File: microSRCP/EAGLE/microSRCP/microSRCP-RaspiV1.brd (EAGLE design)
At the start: 61 x 55.9 mm, 19 parts

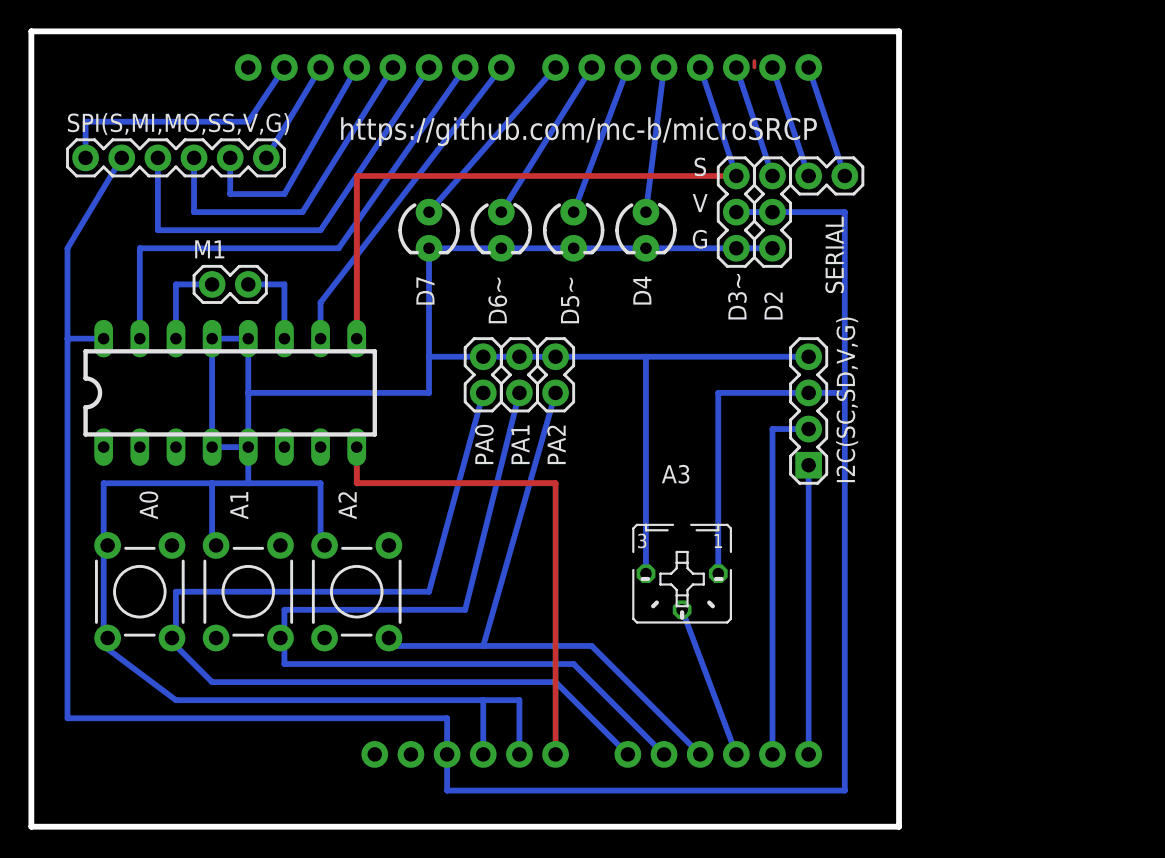
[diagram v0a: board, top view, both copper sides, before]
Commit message: Schaltplaene und Layout von eigenen Shields
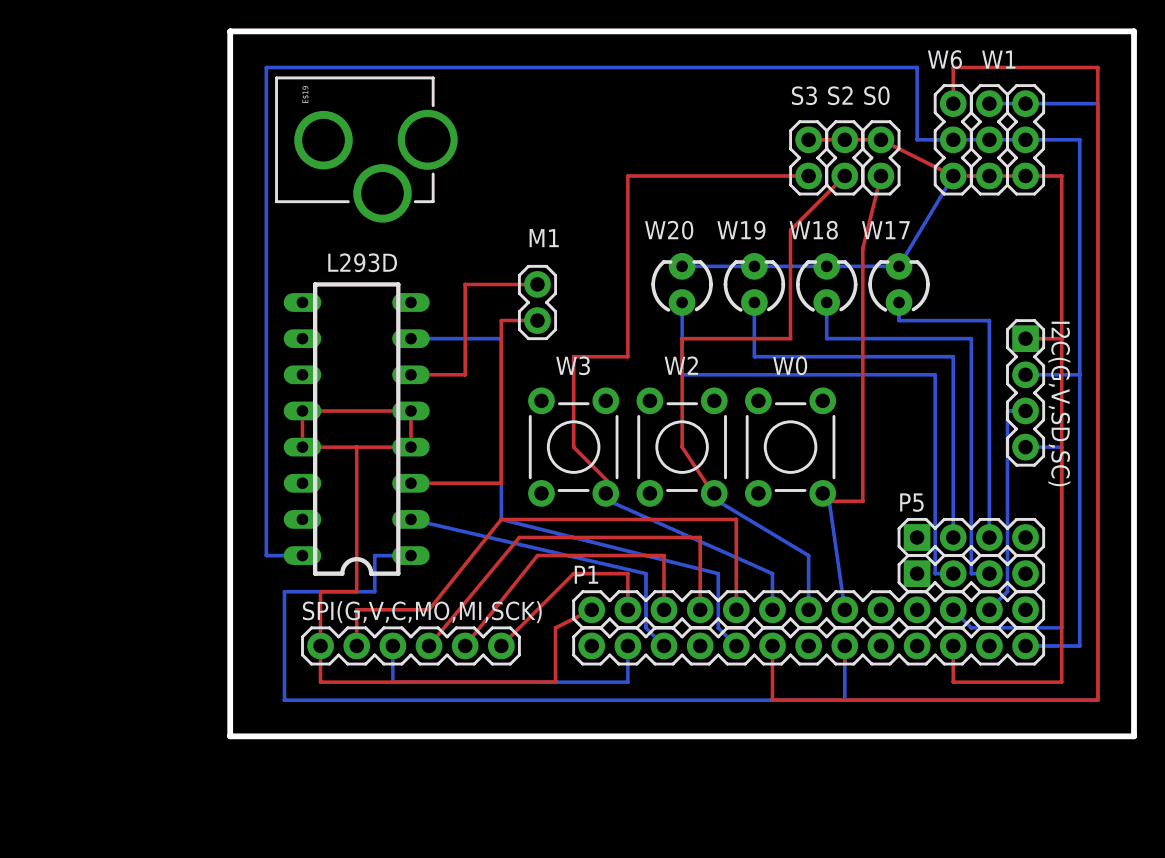
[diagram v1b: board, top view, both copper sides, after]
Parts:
- removed 1: L293D(D3~,D8,D9), SparkFun-AnalogIC:DIL16
- removed 90: (no value), SparkFun-Boards:DUEMILANOVE_SHIELD_NOHOLES_NOLABELS
- removed A0, A1, A2: (no value), SparkFun-Electromechanical:TACTILE-PTH
- removed A3: (no value), pot:B25P
- removed D2, D3~: (no value), SparkFun-Electromechanical:1X03
- removed D4, D5~, D6~, D7: (no value), SparkFun-LED:LED3MM
- removed I2C(SC,SD,V,G): (no value), SparkFun-Connectors:1X04
- removed PA0, PA1, PA2: (no value), SparkFun-Capacitors:1X02
- removed SPI(S,MI,MO,SS,V,G): (no value), SparkFun-Boards:1X06
- added E$1, P1: (no value), SparkFun-Connectors:1X13
- added E$19: (no value), SparkFun-Connectors:POWER_JACK_PTH_LOCK
- added E$3, I2C(G,V,SD,SC), P5: (no value), SparkFun-Connectors:1X04
- added L293D: (no value), SparkFun-DigitalIC:DIL16
- added S0, S2: (no value), SparkFun-Capacitors:1X02
- added SPI(G,V,C,MO,MI,SCK): (no value), SparkFun-Boards:1X06
- added W0, W2, W3: (no value), SparkFun-Electromechanical:TACTILE-PTH
- added W1, W6: (no value), SparkFun-Capacitors:1X03
- added W17, W18, W19, W20: (no value), SparkFun-LED:LED3MM
- added W1N: (no value), SparkFun-Sensors:1X03
- moved M1 22.9 mm to (35.6, 35.6), turned to 270 degrees
- turned S3 to 90 degrees
- renumbered SERIAL to S3
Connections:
- removed net S$12: 90.TX, S3.1
- removed net S$18: 90.A1
- removed net S$22: 1.11, M1.2
- removed net S$25: 1.10, 90.D8
- removed net VIN: 1.8, 90.VIN
- new net S$15: E$1.6, W6.3
- new net S$23: I2C(G,V,SD,SC).3, P1.12
- new net S1: E$1.8, L293D.1, W1.3, W1N.3
- new net VCC: P1.5, SPI(G,V,C,MO,MI,SCK).2
- net 5V: now also E$1.13, I2C(G,V,SD,SC).2, L293D.16, W1.2, W1N.2, W6.2; no longer 1.16, 90.5V, A3.A, D2.2, D3~.2, I2C(SC,SD,V,G).3, SPI(S,MI,MO,SS,V,G).2
- net GND: now also L293D.12, L293D.13, L293D.4, L293D.5, P1.1, SPI(G,V,C,MO,MI,SCK).1; no longer 1.12, 1.13, 1.4, 1.5, 90.GND@0, 90.GND@1, A3.E, D2.1, D3~.1, D4.K, D5~.K, D6~.K, D7.K, I2C(SC,SD,V,G).4, PA0.2, PA1.2, PA2.2
- net GND2: now also E$1.11, I2C(G,V,SD,SC).1, S0.2, S2.2, S3.2, W1.1, W17.K, W18.K, W19.K, W1N.1, W20.K, W6.1; no longer 90.GND@2, SPI(S,MI,MO,SS,V,G).1
- net S$1: now also P5.3, W17.A; no longer 90.D10, SPI(S,MI,MO,SS,V,G).3
- net S$10: now also P1.3, SPI(G,V,C,MO,MI,SCK).5; no longer 90.D2, D2.3
- net S$11: now also E$1.2, SPI(G,V,C,MO,MI,SCK).3; no longer 90.D12, SPI(S,MI,MO,SS,V,G).5
- net S$13: now also E$1.5, L293D.7; no longer 90.RX, S3.2
- net S$14: now also E$1.3, L293D.2; no longer 90.D11, SPI(S,MI,MO,SS,V,G).4
- net S$16: now also L293D.6, M1.1; no longer 90.A4, I2C(SC,SD,V,G).2
- net S$17: now also L293D.3, M1.2; no longer 90.A0, PA0.1
- net S$19: now also S0.1; no longer 90.A2, PA2.1
- net S$2: now also E$3.3, W18.A; no longer 90.A5, I2C(SC,SD,V,G).1
- net S$20: now also S2.1; no longer PA1.1
- net S$21: now also S3.1; no longer 90.A3, A3.S
- net S$24: now also I2C(G,V,SD,SC).4, P1.11; no longer 1.14, M1.1
- net S$3: now also P5.2, W19.A; no longer 1.15, 90.D9
- net S$4: now also E$3.2, W20.A; no longer 90.D13, SPI(S,MI,MO,SS,V,G).6
- net S$5: now also P1.8; no longer 90.D7, D7.A
- net S$6: now also P1.7; no longer 90.D6, D6~.A
- net S$7: now also P1.6; no longer 90.D5, D5~.A
- net S$8: now also P1.4, SPI(G,V,C,MO,MI,SCK).4; no longer 90.D4, D4.A
- net S$9: now also P1.2, SPI(G,V,C,MO,MI,SCK).6; no longer 1.9, 90.D3, D3~.3
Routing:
- net S1: track 0.00 -> 130.8 mm
- net GND: track 184.2 -> 62.5 mm
- net S$15: track 0.00 -> 83.8 mm
- net GND2: track 18.5 -> 89.3 mm
- net S$17: track 71.0 -> 20.3 mm
- net VCC: track 0.00 -> 38.6 mm
- net VIN: track 35.6 -> 0.00 mm
- net S$9: track 46.1 -> 13.5 mm
- net S$13: track 8.03 -> 40.4 mm
- net S$4: track 7.41 -> 38.1 mm
- net S$18: track 30.6 -> 0.00 mm
- net 5V: track 172.5 -> 142.2 mm
- net S$21: track 10.9 -> 39.2 mm
- net S$25: track 23.4 -> 0.00 mm
- net S$19: track 43.2 -> 25.6 mm
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- removed copper zone on layer 1, net GND
- removed copper zone on layer 16, net S$15
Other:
- board size 61 x 55.9 mm -> 63.5 x 49.5 mm
- board text removed: "https://github.com/mc-b/microSRCP"
